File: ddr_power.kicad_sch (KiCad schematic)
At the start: 27 parts, among them U2 MT53D512M32D2DS

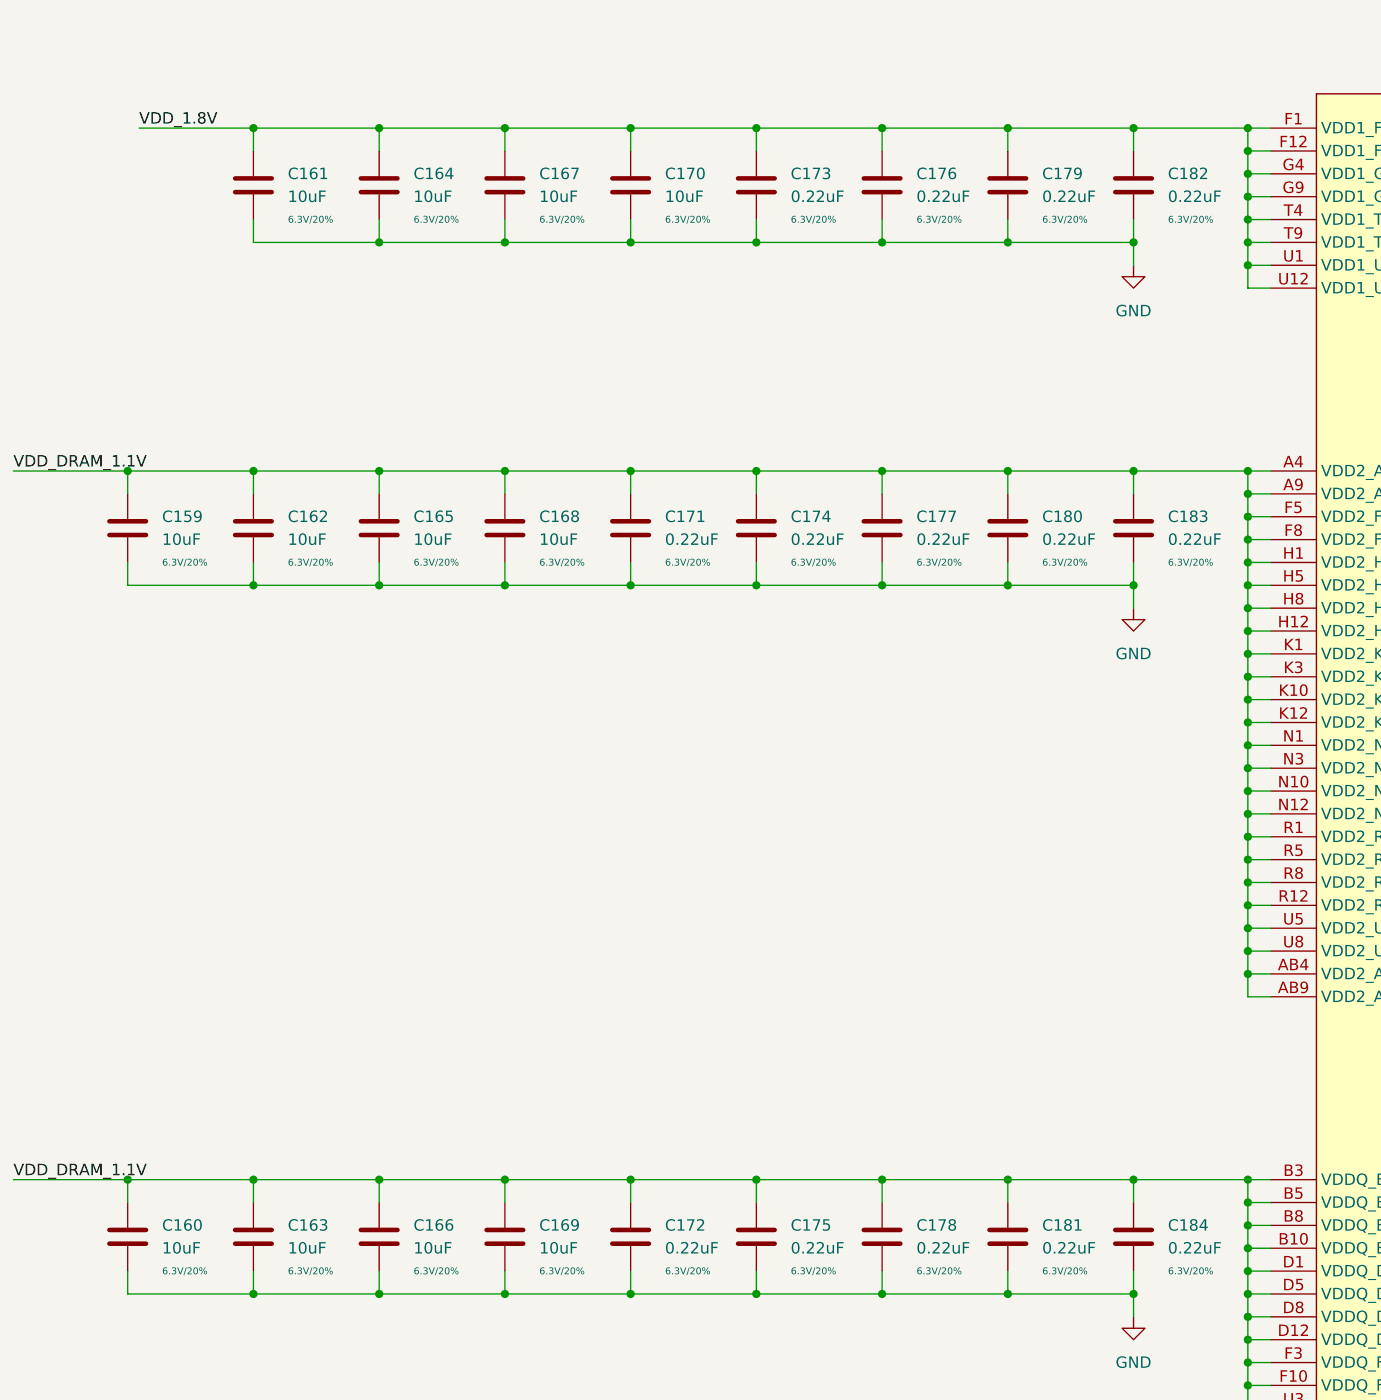
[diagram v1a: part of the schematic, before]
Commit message: add UART4 connector
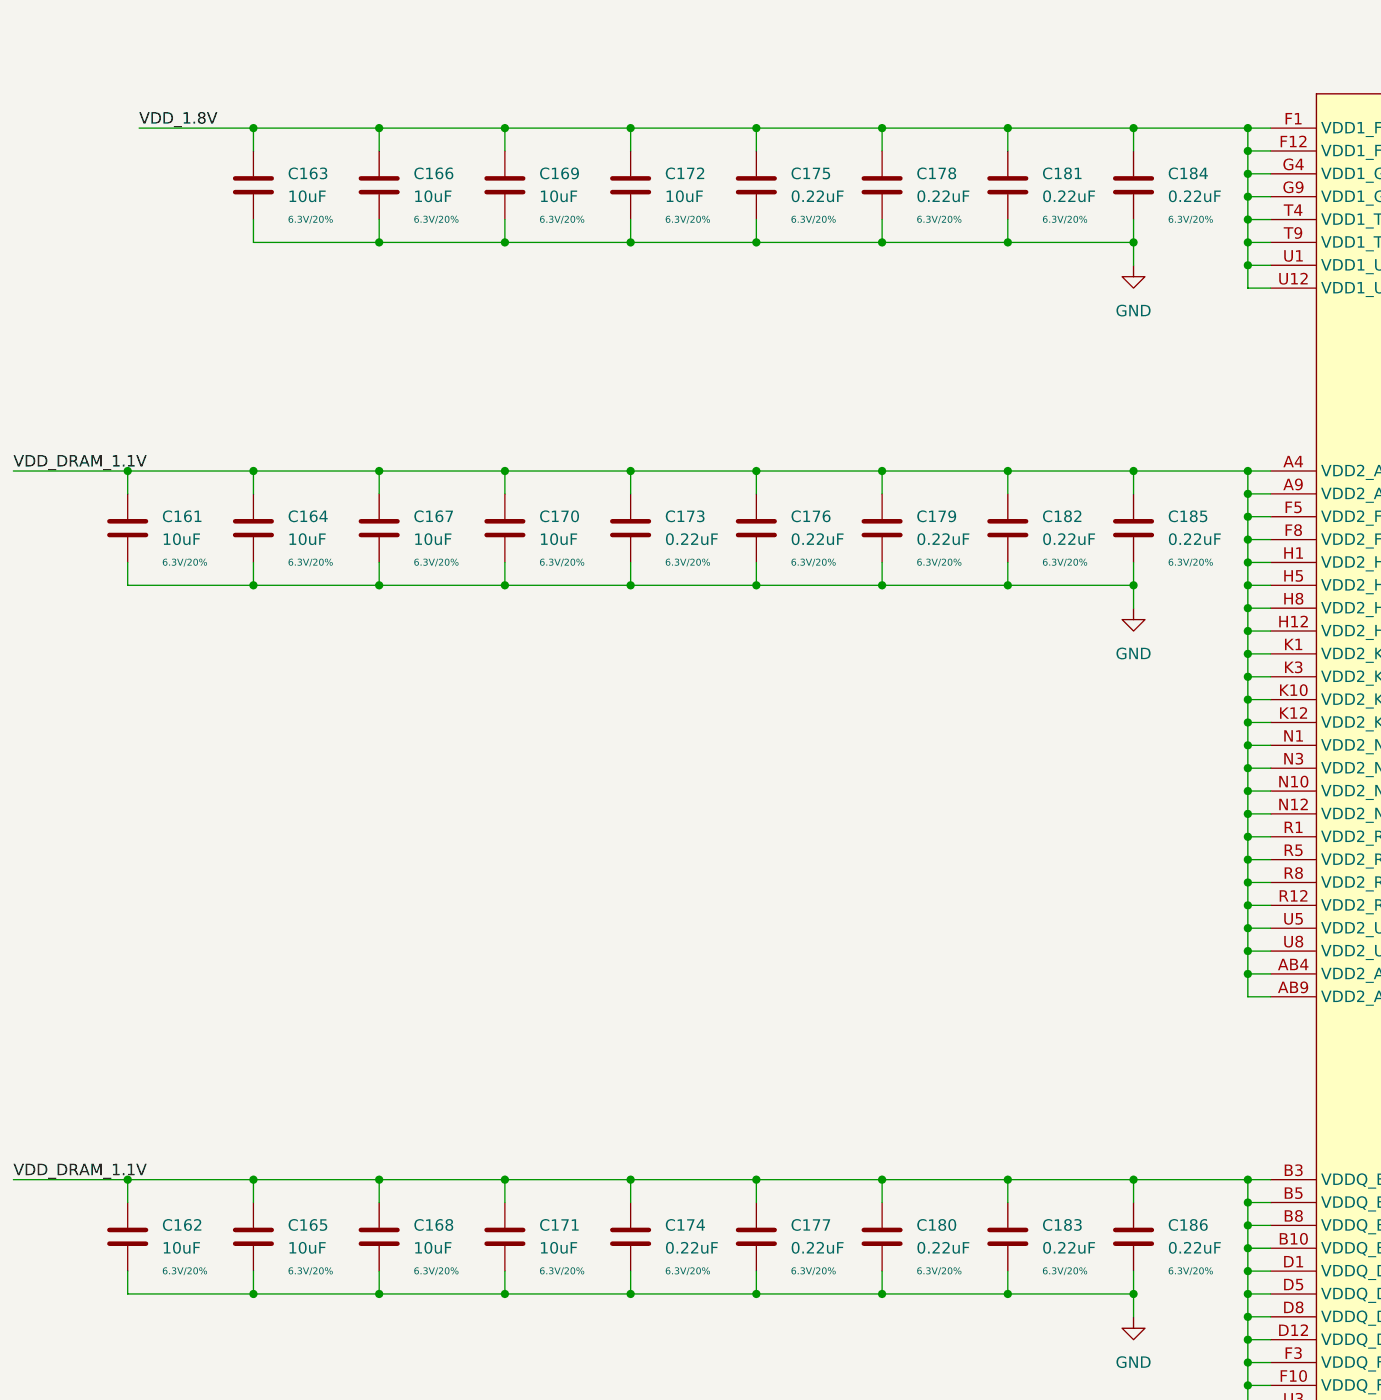
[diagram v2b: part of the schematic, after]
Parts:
- renumbered C159 to C161, C160 to C162, C161 to C163, C162 to C164, C163 to C165, C164 to C166, C165 to C167, C166 to C168, C167 to C169, C168 to C170, C169 to C171, C170 to C172, C171 to C173, C172 to C174, C173 to C175, C174 to C176, C175 to C177, C176 to C178, C177 to C179, C178 to C180, C179 to C181, C180 to C182, C181 to C183, C182 to C184, C183 to C185, C184 to C186
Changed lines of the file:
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@@
   (symbol (lib_id "Device:C") (at 120.65 59.69 0) (unit 1)
     (in_bom yes) (on_board yes)
-    (property "Reference" "C164" (id 0) (at 124.46 58.4199 0)
+    (property "Reference" "C166" (id 0) (at 124.46 58.4199 0)
       (effects (font (size 1.27 1.27)) (justify left))
     )
@@
   (symbol (lib_id "Device:C") (at 190.5 59.69 0) (unit 1)
     (in_bom yes) (on_board yes)
-    (property "Reference" "C179" (id 0) (at 194.31 58.4199 0)
+    (property "Reference" "C181" (id 0) (at 194.31 58.4199 0)
       (effects (font (size 1.27 1.27)) (justify left))
     )
@@
   (symbol (lib_id "Device:C") (at 162.56 97.79 0) (unit 1)
     (in_bom yes) (on_board yes)
-    (property "Reference" "C174" (id 0) (at 166.37 96.5199 0)
+    (property "Reference" "C176" (id 0) (at 166.37 96.5199 0)
       (effects (font (size 1.27 1.27)) (justify left))
     )
@@
   (symbol (lib_id "Device:C") (at 190.5 176.53 0) (unit 1)
     (in_bom yes) (on_board yes)
-    (property "Reference" "C181" (id 0) (at 194.31 175.2599 0)
+    (property "Reference" "C183" (id 0) (at 194.31 175.2599 0)
       (effects (font (size 1.27 1.27)) (justify left))
     )
@@
   (symbol (lib_id "Device:C") (at 148.59 59.69 0) (unit 1)
     (in_bom yes) (on_board yes)
-    (property "Reference" "C170" (id 0) (at 152.4 58.4199 0)
+    (property "Reference" "C172" (id 0) (at 152.4 58.4199 0)
       (effects (font (size 1.27 1.27)) (justify left))
     )
@@
   (symbol (lib_id "Device:C") (at 190.5 97.79 0) (unit 1)
     (in_bom yes) (on_board yes)
-    (property "Reference" "C180" (id 0) (at 194.31 96.5199 0)
+    (property "Reference" "C182" (id 0) (at 194.31 96.5199 0)
       (effects (font (size 1.27 1.27)) (justify left))
     )
@@
   (symbol (lib_id "Device:C") (at 176.53 59.69 0) (unit 1)
     (in_bom yes) (on_board yes)
-    (property "Reference" "C176" (id 0) (at 180.34 58.4199 0)
+    (property "Reference" "C178" (id 0) (at 180.34 58.4199 0)
       (effects (font (size 1.27 1.27)) (justify left))
     )
@@
   (symbol (lib_id "power:GND") (at 204.47 68.58 0) (unit 1)
     (in_bom yes) (on_board yes) (fields_autoplaced)
-    (property "Reference" "#PWR0150" (id 0) (at 204.47 74.93 0)
+    (property "Reference" "#PWR0153" (id 0) (at 204.47 74.93 0)
       (effects (font (size 1.27 1.27)) hide)
     )
@@
   (symbol (lib_id "Device:C") (at 134.62 59.69 0) (unit 1)
     (in_bom yes) (on_board yes)
-    (property "Reference" "C167" (id 0) (at 138.43 58.4199 0)
+    (property "Reference" "C169" (id 0) (at 138.43 58.4199 0)
       (effects (font (size 1.27 1.27)) (justify left))
     )
@@
   (symbol (lib_id "Device:C") (at 204.47 176.53 0) (unit 1)
     (in_bom yes) (on_board yes)
-    (property "Reference" "C184" (id 0) (at 208.28 175.2599 0)
+    (property "Reference" "C186" (id 0) (at 208.28 175.2599 0)
       (effects (font (size 1.27 1.27)) (justify left))
     )
@@
   (symbol (lib_id "Device:C") (at 92.71 176.53 0) (unit 1)
     (in_bom yes) (on_board yes)
-    (property "Reference" "C160" (id 0) (at 96.52 175.2599 0)
+    (property "Reference" "C162" (id 0) (at 96.52 175.2599 0)
       (effects (font (size 1.27 1.27)) (justify left))
     )
@@
   (symbol (lib_id "Device:C") (at 204.47 97.79 0) (unit 1)
     (in_bom yes) (on_board yes)
-    (property "Reference" "C183" (id 0) (at 208.28 96.5199 0)
+    (property "Reference" "C185" (id 0) (at 208.28 96.5199 0)
       (effects (font (size 1.27 1.27)) (justify left))
     )
@@
   (symbol (lib_id "Device:C") (at 204.47 59.69 0) (unit 1)
     (in_bom yes) (on_board yes)
-    (property "Reference" "C182" (id 0) (at 208.28 58.4199 0)
+    (property "Reference" "C184" (id 0) (at 208.28 58.4199 0)
       (effects (font (size 1.27 1.27)) (justify left))
     )
@@
   (symbol (lib_id "Device:C") (at 120.65 97.79 0) (unit 1)
     (in_bom yes) (on_board yes)
-    (property "Reference" "C165" (id 0) (at 124.46 96.5199 0)
+    (property "Reference" "C167" (id 0) (at 124.46 96.5199 0)
       (effects (font (size 1.27 1.27)) (justify left))
     )
@@
   (symbol (lib_id "Device:C") (at 176.53 176.53 0) (unit 1)
     (in_bom yes) (on_board yes)
-    (property "Reference" "C178" (id 0) (at 180.34 175.2599 0)
+    (property "Reference" "C180" (id 0) (at 180.34 175.2599 0)
       (effects (font (size 1.27 1.27)) (justify left))
     )
@@
   (symbol (lib_id "power:GND") (at 204.47 106.68 0) (unit 1)
     (in_bom yes) (on_board yes) (fields_autoplaced)
-    (property "Reference" "#PWR0151" (id 0) (at 204.47 113.03 0)
+    (property "Reference" "#PWR0154" (id 0) (at 204.47 113.03 0)
       (effects (font (size 1.27 1.27)) hide)
     )
@@
   (symbol (lib_id "power:GND") (at 204.47 185.42 0) (unit 1)
     (in_bom yes) (on_board yes) (fields_autoplaced)
-    (property "Reference" "#PWR0152" (id 0) (at 204.47 191.77 0)
+    (property "Reference" "#PWR0155" (id 0) (at 204.47 191.77 0)
       (effects (font (size 1.27 1.27)) hide)
     )
@@
   (symbol (lib_id "Device:C") (at 162.56 59.69 0) (unit 1)
     (in_bom yes) (on_board yes)
-    (property "Reference" "C173" (id 0) (at 166.37 58.4199 0)
+    (property "Reference" "C175" (id 0) (at 166.37 58.4199 0)
       (effects (font (size 1.27 1.27)) (justify left))
     )
@@
   (symbol (lib_id "Device:C") (at 148.59 97.79 0) (unit 1)
     (in_bom yes) (on_board yes)
-    (property "Reference" "C171" (id 0) (at 152.4 96.5199 0)
+    (property "Reference" "C173" (id 0) (at 152.4 96.5199 0)
       (effects (font (size 1.27 1.27)) (justify left))
     )
@@
   (symbol (lib_id "Device:C") (at 106.68 59.69 0) (unit 1)
     (in_bom yes) (on_board yes)
-    (property "Reference" "C161" (id 0) (at 110.49 58.4199 0)
+    (property "Reference" "C163" (id 0) (at 110.49 58.4199 0)
       (effects (font (size 1.27 1.27)) (justify left))
     )
@@
   (symbol (lib_id "power:GND") (at 283.21 200.66 0) (unit 1)
     (in_bom yes) (on_board yes) (fields_autoplaced)
-    (property "Reference" "#PWR0153" (id 0) (at 283.21 207.01 0)
+    (property "Reference" "#PWR0156" (id 0) (at 283.21 207.01 0)
       (effects (font (size 1.27 1.27)) hide)
     )
@@
   (symbol (lib_id "Device:C") (at 106.68 176.53 0) (unit 1)
     (in_bom yes) (on_board yes)
-    (property "Reference" "C163" (id 0) (at 110.49 175.2599 0)
+    (property "Reference" "C165" (id 0) (at 110.49 175.2599 0)
       (effects (font (size 1.27 1.27)) (justify left))
     )
@@
   (symbol (lib_id "Device:C") (at 134.62 176.53 0) (unit 1)
     (in_bom yes) (on_board yes)
-    (property "Reference" "C169" (id 0) (at 138.43 175.2599 0)
+    (property "Reference" "C171" (id 0) (at 138.43 175.2599 0)
       (effects (font (size 1.27 1.27)) (justify left))
     )
@@
   (symbol (lib_id "Device:C") (at 148.59 176.53 0) (unit 1)
     (in_bom yes) (on_board yes)
-    (property "Reference" "C172" (id 0) (at 152.4 175.2599 0)
+    (property "Reference" "C174" (id 0) (at 152.4 175.2599 0)
       (effects (font (size 1.27 1.27)) (justify left))
     )
@@
   (symbol (lib_id "Device:C") (at 134.62 97.79 0) (unit 1)
     (in_bom yes) (on_board yes)
-    (property "Reference" "C168" (id 0) (at 138.43 96.5199 0)
+    (property "Reference" "C170" (id 0) (at 138.43 96.5199 0)
       (effects (font (size 1.27 1.27)) (justify left))
     )
@@
   (symbol (lib_id "Device:C") (at 106.68 97.79 0) (unit 1)
     (in_bom yes) (on_board yes)
-    (property "Reference" "C162" (id 0) (at 110.49 96.5199 0)
+    (property "Reference" "C164" (id 0) (at 110.49 96.5199 0)
       (effects (font (size 1.27 1.27)) (justify left))
     )
@@
   (symbol (lib_id "Device:C") (at 162.56 176.53 0) (unit 1)
     (in_bom yes) (on_board yes)
-    (property "Reference" "C175" (id 0) (at 166.37 175.2599 0)
+    (property "Reference" "C177" (id 0) (at 166.37 175.2599 0)
       (effects (font (size 1.27 1.27)) (justify left))
     )
@@
   (symbol (lib_id "Device:C") (at 120.65 176.53 0) (unit 1)
     (in_bom yes) (on_board yes)
-    (property "Reference" "C166" (id 0) (at 124.46 175.2599 0)
+    (property "Reference" "C168" (id 0) (at 124.46 175.2599 0)
       (effects (font (size 1.27 1.27)) (justify left))
     )
@@
   (symbol (lib_id "Device:C") (at 176.53 97.79 0) (unit 1)
     (in_bom yes) (on_board yes)
-    (property "Reference" "C177" (id 0) (at 180.34 96.5199 0)
+    (property "Reference" "C179" (id 0) (at 180.34 96.5199 0)
       (effects (font (size 1.27 1.27)) (justify left))
     )
@@
   (symbol (lib_id "Device:C") (at 92.71 97.79 0) (unit 1)
     (in_bom yes) (on_board yes)
-    (property "Reference" "C159" (id 0) (at 96.52 96.5199 0)
-      (effects (font (size 1.27 1.27)) (justify left))
-    )
+    (property "Reference" "C161" (id 0) (at 96.52 96.5199 0)
+      (effects (font (size 1.27 1.27)) (justify left))
+    )

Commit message: change USB-UART conn, add new 0402 fp, more pcb work
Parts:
- C161, C162, C163, C164, C165, C166, C167, C168, C169, C170, C171, C172: footprint Capacitor_SMD:C_0402_1005Metric -> qsbc:C_0402_1005Metric
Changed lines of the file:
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@@
       (effects (font (size 1.27 1.27)) (justify left))
     )
-    (property "Footprint" "Capacitor_SMD:C_0402_1005Metric" (id 2) (at 121.6152 63.5 0)
+    (property "Footprint" "qsbc:C_0402_1005Metric" (id 2) (at 121.6152 63.5 0)
       (effects (font (size 1.27 1.27)) hide)
     )
@@
       (effects (font (size 1.27 1.27)) (justify left))
     )
-    (property "Footprint" "Capacitor_SMD:C_0402_1005Metric" (id 2) (at 149.5552 63.5 0)
+    (property "Footprint" "qsbc:C_0402_1005Metric" (id 2) (at 149.5552 63.5 0)
       (effects (font (size 1.27 1.27)) hide)
     )
@@
       (effects (font (size 1.27 1.27)) (justify left))
     )
-    (property "Footprint" "Capacitor_SMD:C_0402_1005Metric" (id 2) (at 135.5852 63.5 0)
+    (property "Footprint" "qsbc:C_0402_1005Metric" (id 2) (at 135.5852 63.5 0)
       (effects (font (size 1.27 1.27)) hide)
     )
@@
       (effects (font (size 1.27 1.27)) (justify left))
     )
-    (property "Footprint" "Capacitor_SMD:C_0402_1005Metric" (id 2) (at 93.6752 180.34 0)
+    (property "Footprint" "qsbc:C_0402_1005Metric" (id 2) (at 93.6752 180.34 0)
       (effects (font (size 1.27 1.27)) hide)
     )
@@
       (effects (font (size 1.27 1.27)) (justify left))
     )
-    (property "Footprint" "Capacitor_SMD:C_0402_1005Metric" (id 2) (at 121.6152 101.6 0)
+    (property "Footprint" "qsbc:C_0402_1005Metric" (id 2) (at 121.6152 101.6 0)
       (effects (font (size 1.27 1.27)) hide)
     )
@@
       (effects (font (size 1.27 1.27)) (justify left))
     )
-    (property "Footprint" "Capacitor_SMD:C_0402_1005Metric" (id 2) (at 107.6452 63.5 0)
+    (property "Footprint" "qsbc:C_0402_1005Metric" (id 2) (at 107.6452 63.5 0)
       (effects (font (size 1.27 1.27)) hide)
     )
@@
       (effects (font (size 1.27 1.27)) (justify left))
     )
-    (property "Footprint" "Capacitor_SMD:C_0402_1005Metric" (id 2) (at 107.6452 180.34 0)
+    (property "Footprint" "qsbc:C_0402_1005Metric" (id 2) (at 107.6452 180.34 0)
       (effects (font (size 1.27 1.27)) hide)
     )
@@
       (effects (font (size 1.27 1.27)) (justify left))
     )
-    (property "Footprint" "Capacitor_SMD:C_0402_1005Metric" (id 2) (at 135.5852 180.34 0)
+    (property "Footprint" "qsbc:C_0402_1005Metric" (id 2) (at 135.5852 180.34 0)
       (effects (font (size 1.27 1.27)) hide)
     )
@@
       (effects (font (size 1.27 1.27)) (justify left))
     )
-    (property "Footprint" "Capacitor_SMD:C_0402_1005Metric" (id 2) (at 135.5852 101.6 0)
+    (property "Footprint" "qsbc:C_0402_1005Metric" (id 2) (at 135.5852 101.6 0)
       (effects (font (size 1.27 1.27)) hide)
     )
@@
       (effects (font (size 1.27 1.27)) (justify left))
     )
-    (property "Footprint" "Capacitor_SMD:C_0402_1005Metric" (id 2) (at 107.6452 101.6 0)
+    (property "Footprint" "qsbc:C_0402_1005Metric" (id 2) (at 107.6452 101.6 0)
       (effects (font (size 1.27 1.27)) hide)
     )
@@
       (effects (font (size 1.27 1.27)) (justify left))
     )
-    (property "Footprint" "Capacitor_SMD:C_0402_1005Metric" (id 2) (at 121.6152 180.34 0)
+    (property "Footprint" "qsbc:C_0402_1005Metric" (id 2) (at 121.6152 180.34 0)
       (effects (font (size 1.27 1.27)) hide)
     )
@@
       (effects (font (size 1.27 1.27)) (justify left))
     )
-    (property "Footprint" "Capacitor_SMD:C_0402_1005Metric" (id 2) (at 93.6752 101.6 0)
-      (effects (font (size 1.27 1.27)) hide)
-    )
+    (property "Footprint" "qsbc:C_0402_1005Metric" (id 2) (at 93.6752 101.6 0)
+      (effects (font (size 1.27 1.27)) hide)
+    )
